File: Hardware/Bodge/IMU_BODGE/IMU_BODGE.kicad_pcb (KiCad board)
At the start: 2 copper layers, 9 x 6.7 mm, 10 parts, among them U1 ICM-20602

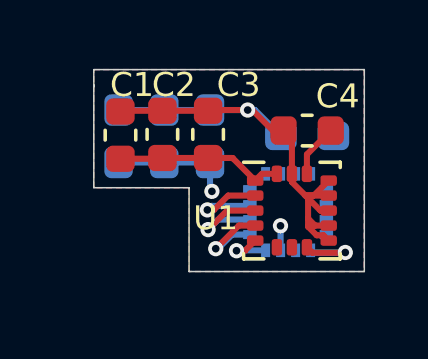
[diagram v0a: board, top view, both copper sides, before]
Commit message: Fixed design rules
Design rules were not auto applying.
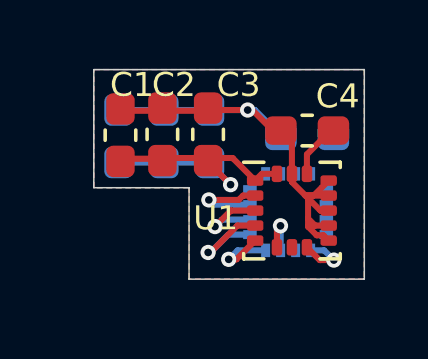
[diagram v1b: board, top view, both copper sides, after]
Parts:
- C1, C2, C3, C4: footprint Capacitor_SMD:C_0603_1608Metric -> Capacitor_SMD:C_0603_1608Metric_Pad1.05x0.95mm_HandSolder
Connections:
- REF** pad 1: /REGOUT -> (no net)
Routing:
- net /IMU_VDC: track 9.67 -> 10.9 mm
- net /INT: track 0.82 -> 1.59 mm
- net /NSS: track 1.74 -> 2.50 mm
- net /MISO: track 2.97 -> 3.58 mm
- net /FSYNC: track 2.54 -> 1.98 mm
- net /MOSI: track 3.36 -> 2.82 mm
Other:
- board size 9 x 6.7 mm -> 9 x 7 mm

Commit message: Solder Design Changes
Changed the vias for improved thermal transfer.
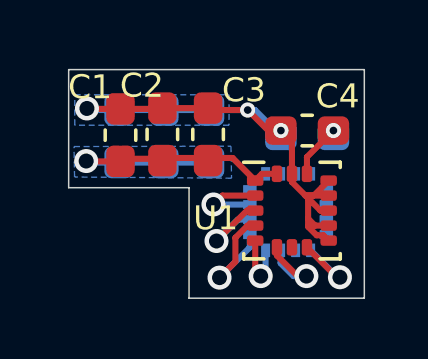
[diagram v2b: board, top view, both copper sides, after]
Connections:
- REF** pad 1: (no net) -> /REGOUT
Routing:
- net GND: track 19.3 -> 21.6 mm, vias 1 -> 3
- net /INT: track 1.59 -> 3.01 mm
- net /FSYNC: track 1.98 -> 2.86 mm
- net /MISO: track 3.58 -> 4.23 mm
- net /REGOUT: track 1.77 -> 1.81 mm, vias 0 -> 1
- added copper zone on B.Cu, net /IMU_VDC
- removed copper zone on F.Cu, net GND
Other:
- board size 9 x 7 mm -> 9.9 x 7.6 mm
- net class Default: via_dia 0.508 -> 0.8; via_drill 0.254 -> 0.5
